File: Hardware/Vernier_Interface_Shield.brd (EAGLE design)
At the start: 42 parts, among them U1 74HC4052SO, U2 LMV358

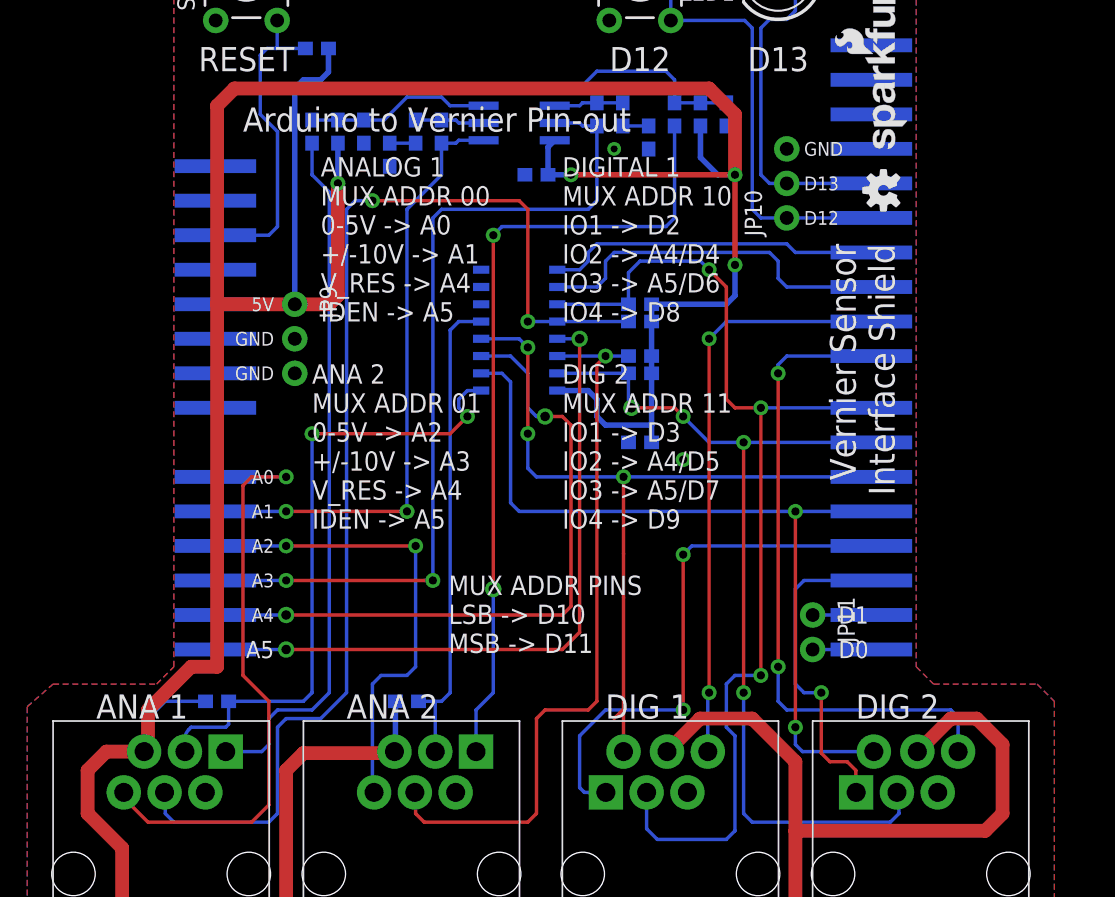
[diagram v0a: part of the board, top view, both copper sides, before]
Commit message: Changed Pins 2 and 3 to BTD connector 1
Changed circuit so that Pins 2 and 3 are connected to BTD 1 - allows for
use of Hardware interrupts from Arduino.

Also cleaned up silks
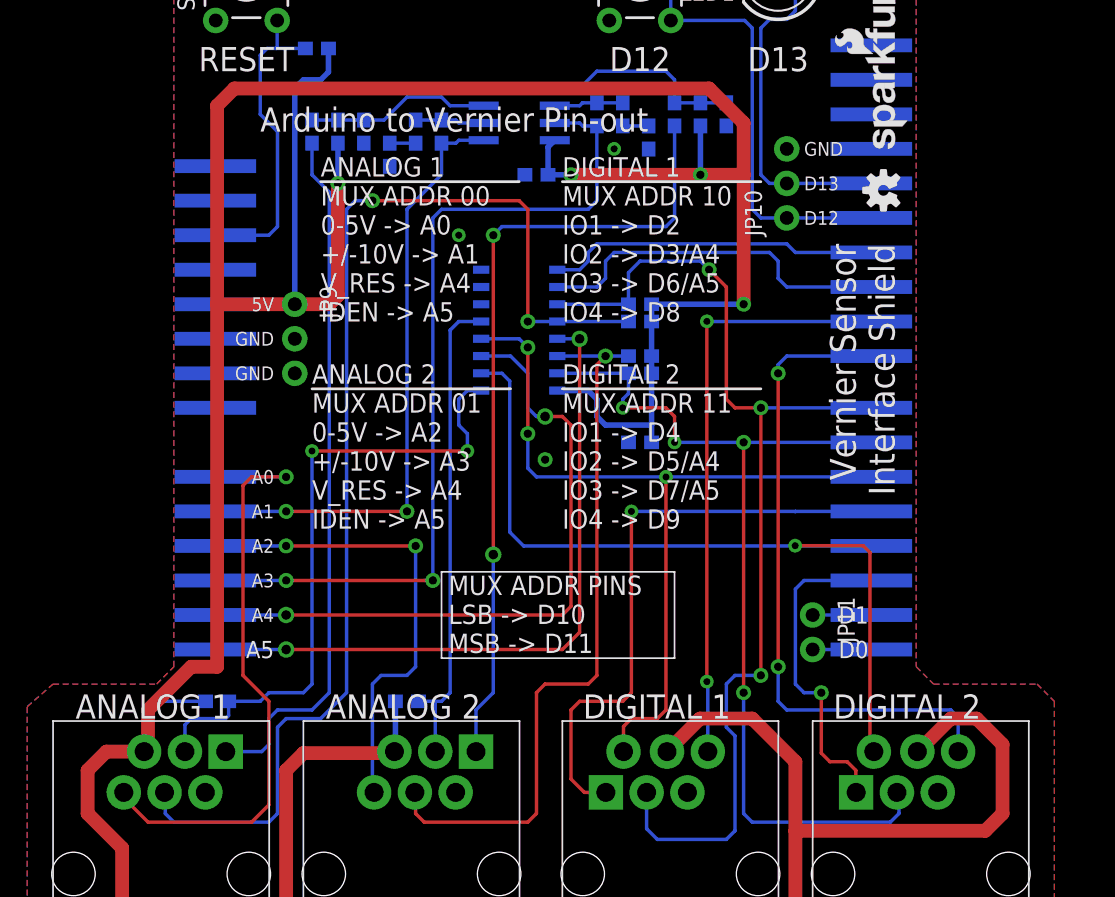
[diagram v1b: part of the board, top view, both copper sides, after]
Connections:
- net N$24 renamed AS1_VRES
- net D1_IO2: now also JP2.4; no longer JP2.5
- net D2_IO1: now also JP2.5; no longer JP2.4
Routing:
- net D2_IO1: track 39.8 -> 44.0 mm, vias 2 -> 1
- net 5V: track 346.6 -> 349.0 mm
- net D1_IO3: track 67.5 -> 69.3 mm
- net D2_IO2: track 59.3 -> 60.7 mm
- net D2_IO4: track 42.9 -> 43.8 mm
- net D1_IO2: track 61.3 -> 61.0 mm, vias 2 -> 1
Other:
- board text added: "ANALOG 1"
- board text added: "ANALOG 2"
- board text added: "ANALOG 2 MUX ADDR 01 0-5V -> A2 +/-10V -> A3 V_RES -> A4 IDEN -> A5"
- board text added: "DIGITAL 1"
- board text added: "DIGITAL 1 MUX ADDR 10 IO1 -> D2 IO2 -> D3/A4 IO3 -> D6/A5 IO4 -> D8"
- board text added: "DIGITAL 2"
- board text added: "DIGITAL 2 MUX ADDR 11 IO1 -> D4 IO2 -> D5/A4 IO3 -> D7/A5 IO4 -> D9"
- board text removed: "ANA 1"
- board text removed: "ANA 2"
- board text removed: "ANA 2 MUX ADDR 01 0-5V -> A2 +/-10V -> A3 V_RES -> A4 IDEN -> A5"
- board text removed: "DIG 1"
- board text removed: "DIG 2"
- board text removed: "DIG 2 MUX ADDR 11 IO1 -> D3 IO2 -> A4/D5 IO3 -> A5/D7 IO4 -> D9"
- board text removed: "DIGITAL 1 MUX ADDR 10 IO1 -> D2 IO2 -> A4/D4 IO3 -> A5/D6 IO4 -> D8"

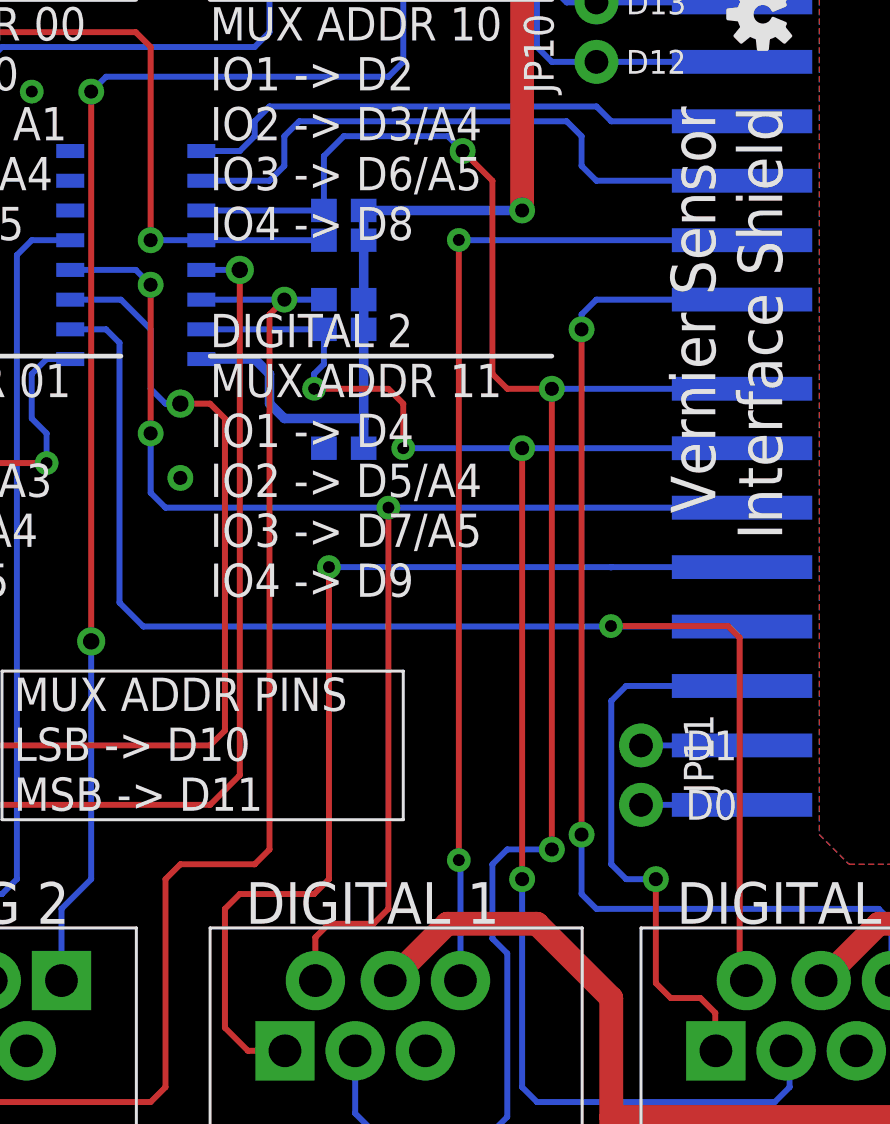
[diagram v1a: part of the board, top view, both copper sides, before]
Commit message: Changed pins one last time...
Changed Digital Pins so that it's pins 2, 3, 4, 5 on Dig 1 and 6, 7, 8
,9 on Dig 2
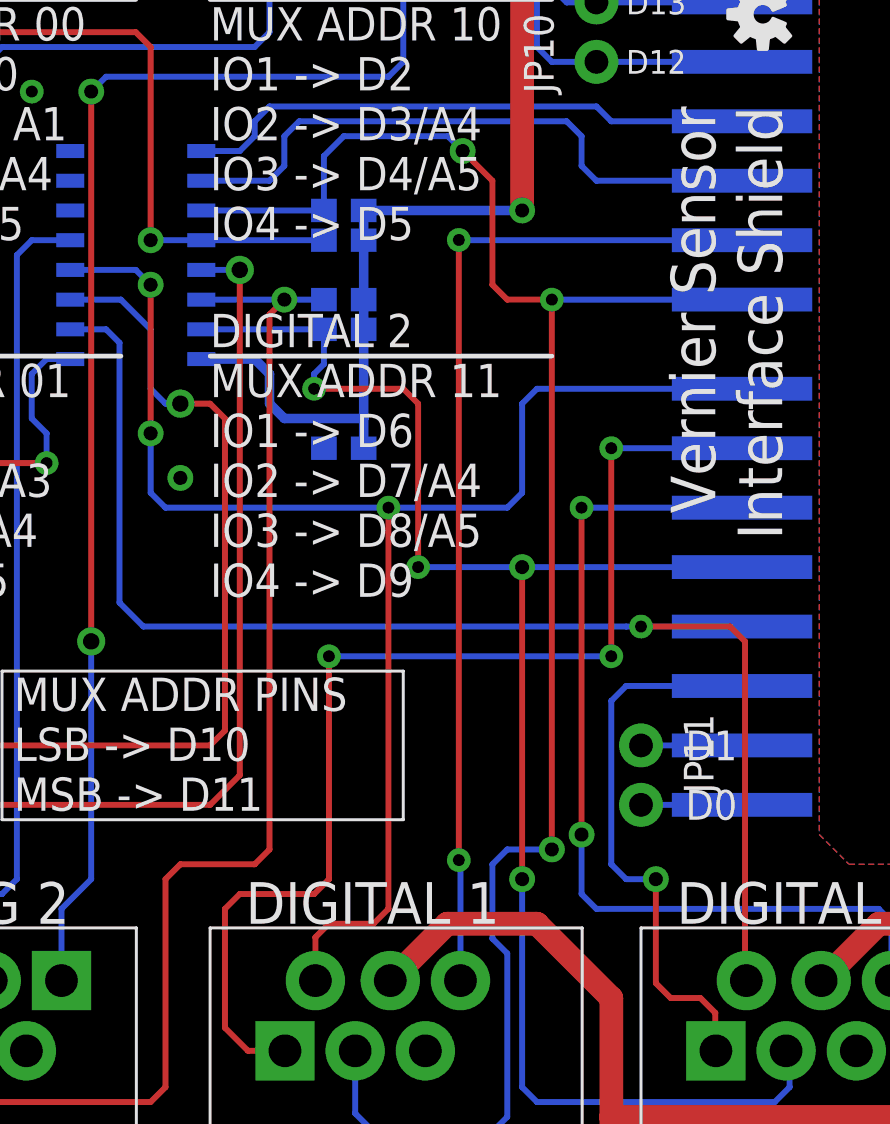
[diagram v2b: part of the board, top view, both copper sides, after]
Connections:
- net D1_IO3: now also JP2.5; no longer JP2.7
- net D1_IO4: now also JP2.6; no longer JP1.1
- net D2_IO1: now also JP2.7; no longer JP2.5
- net D2_IO2: now also JP2.8; no longer JP2.6
- net D2_IO3: now also JP1.1; no longer JP2.8
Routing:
- net D1_IO4: track 48.1 -> 39.6 mm
- net D2_IO1: track 44.0 -> 49.1 mm, vias 1 -> 3
- net D2_IO2: track 60.7 -> 65.1 mm
- net D1_IO2: track 61.0 -> 59.7 mm
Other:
- board text added: "DIGITAL 1 MUX ADDR 10 IO1 -> D2 IO2 -> D3/A4 IO3 -> D4/A5 IO4 -> D5"
- board text added: "DIGITAL 2 MUX ADDR 11 IO1 -> D6 IO2 -> D7/A4 IO3 -> D8/A5 IO4 -> D9"
- board text removed: "DIGITAL 1 MUX ADDR 10 IO1 -> D2 IO2 -> D3/A4 IO3 -> D6/A5 IO4 -> D8"
- board text removed: "DIGITAL 2 MUX ADDR 11 IO1 -> D4 IO2 -> D5/A4 IO3 -> D7/A5 IO4 -> D9"

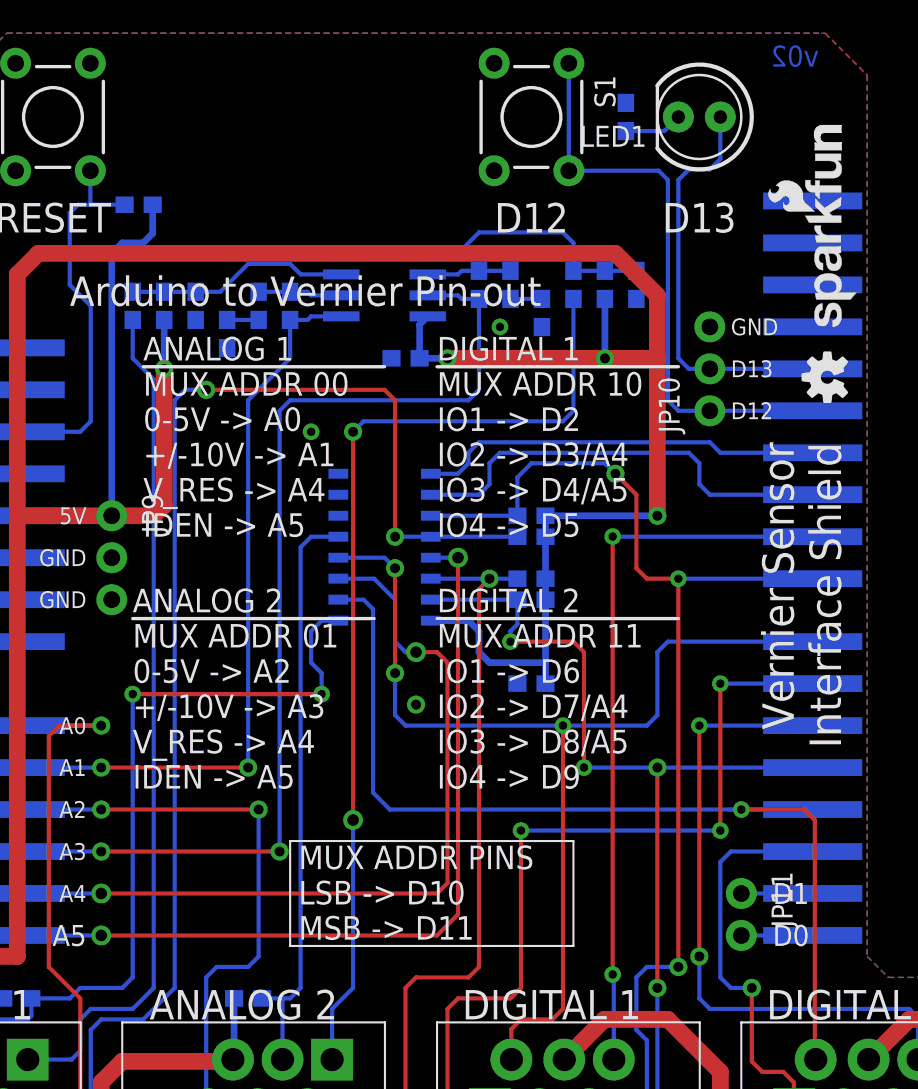
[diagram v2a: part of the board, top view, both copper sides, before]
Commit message: Updated revision code - ready for protos
Hopefully the last round of protos for this board. - Updated silks,
moved VIAS so as not to interfere with printing.
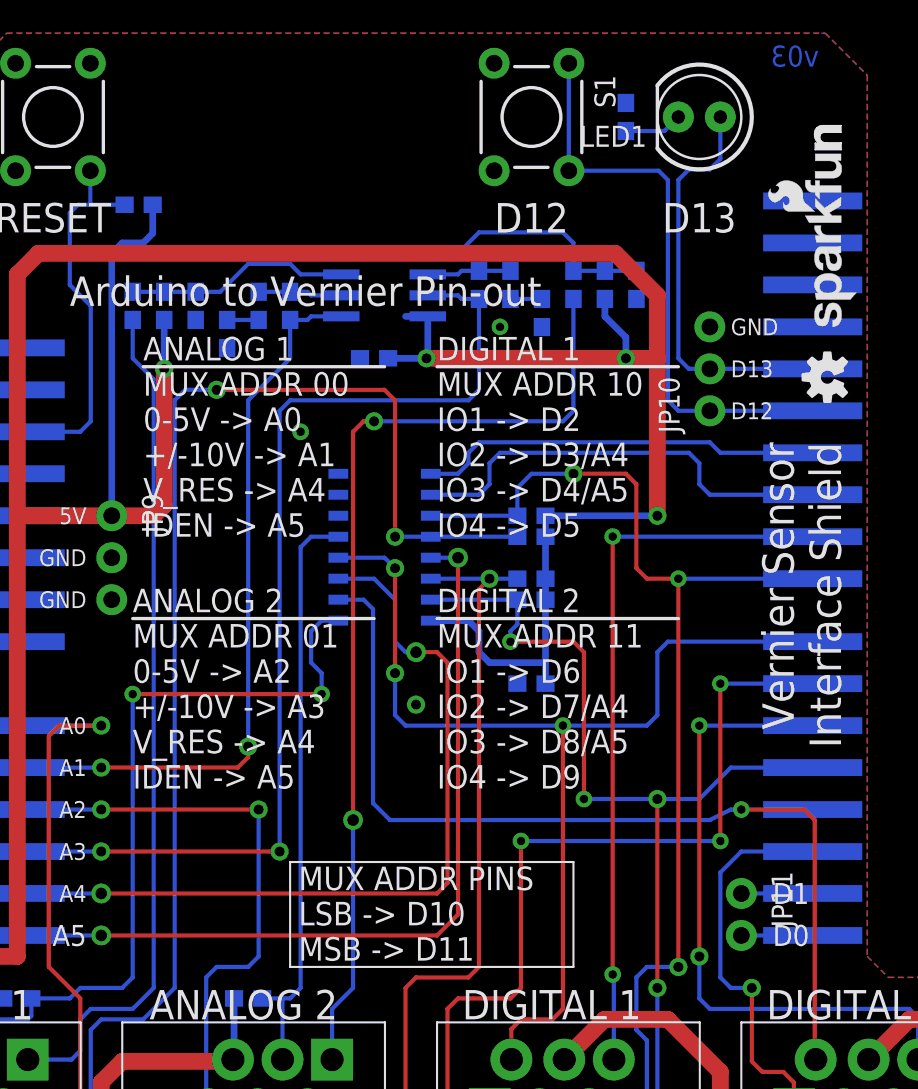
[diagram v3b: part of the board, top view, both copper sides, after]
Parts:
- moved C1 1.91 mm to (35.6, 57.8)
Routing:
- net 5V: track 349.0 -> 351.3 mm
- net D1_IO3: track 69.3 -> 70.1 mm
- net D1_IO2: track 59.7 -> 60.5 mm
- net D2_IO3: track 78.4 -> 77.9 mm
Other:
- board text added: "v03"
- board text removed: "v02"

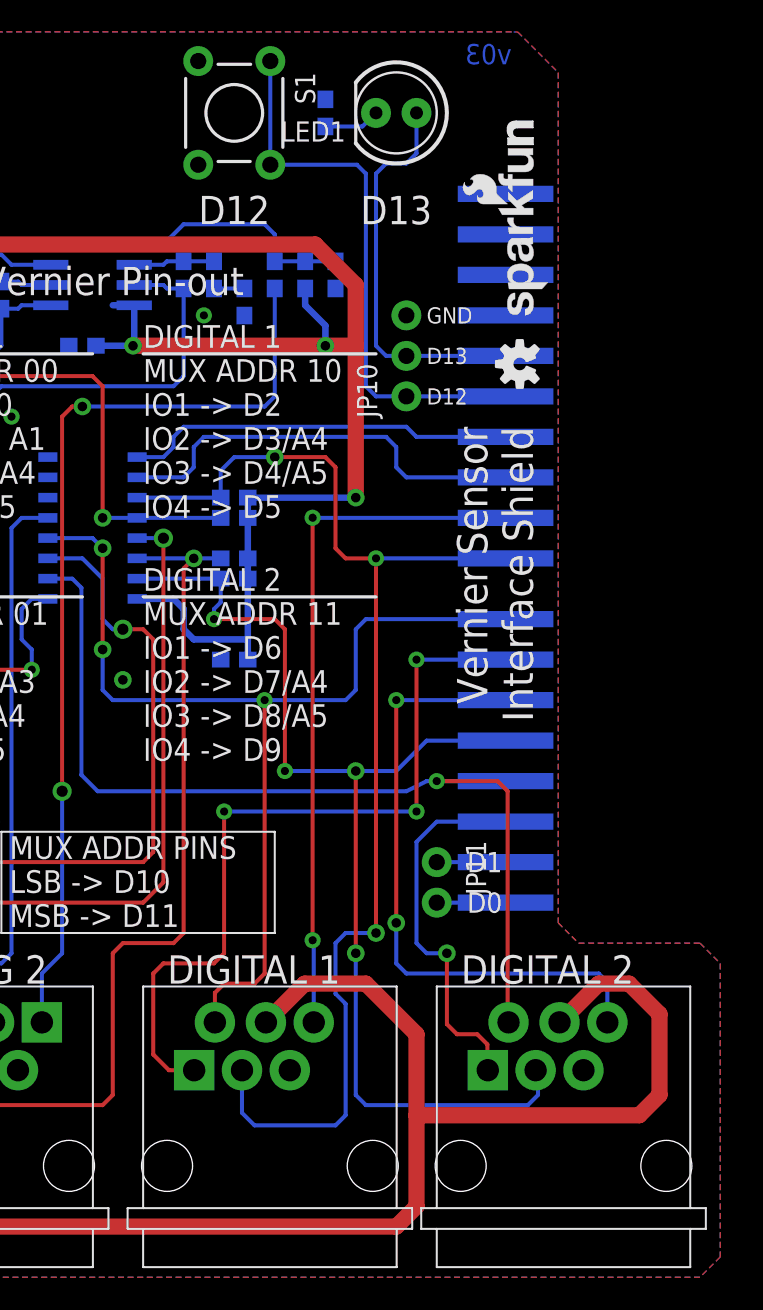
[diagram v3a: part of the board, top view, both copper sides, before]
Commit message: Switched Digital 1 and Digital 2 on the Board
Fixed the Digital 1 and Digital 2. V03 had the two connectors flipped.
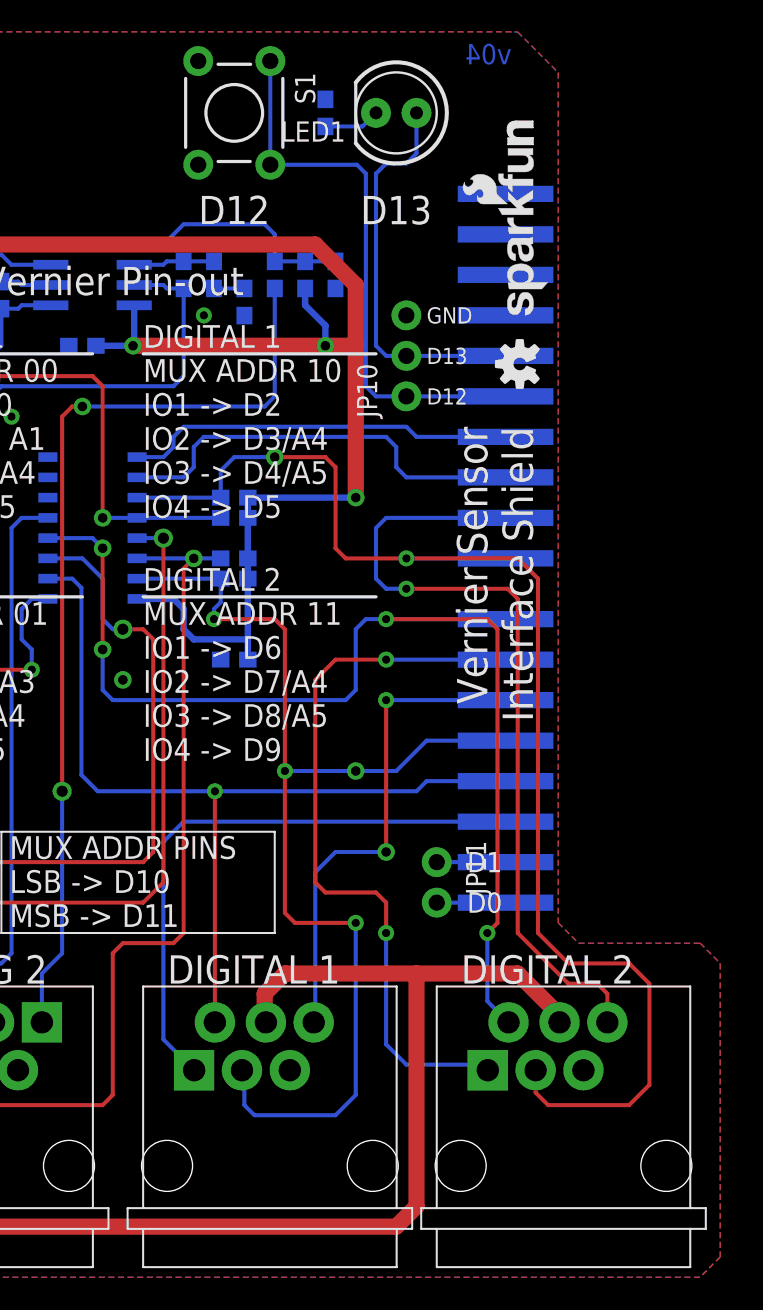
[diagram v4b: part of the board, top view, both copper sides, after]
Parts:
- moved JP7 18.4 mm to (39.4, 0.00)
- moved JP8 18.4 mm to (57.8, 0.00)
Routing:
- net 5V: track 351.3 -> 335.5 mm
- net D1_IO1: track 23.8 -> 37.1 mm, vias 1 -> 0
- net D2_IO2: track 65.1 -> 75.3 mm, vias 3 -> 4
- net D1_IO4: track 39.6 -> 31.4 mm
- net D2_IO3: track 77.9 -> 85.8 mm, vias 3 -> 2
- net D2_IO4: track 43.8 -> 50.9 mm, vias 2 -> 1
- net D1_IO2: track 60.5 -> 55.9 mm
- net D2_IO1: track 49.1 -> 46.1 mm, vias 3 -> 2
- net D1_IO3: track 70.1 -> 70.6 mm
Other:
- board text added: "v04"
- board text removed: "v03"
